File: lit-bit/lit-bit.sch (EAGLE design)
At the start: 71 parts, among them J2 USB_MICRO_B_SMD_FEMALE, J3 ISP, U2 32U4, U3 73831, U4 ADXL345, U5 S-1335, U6 MCP7940N, U7 24FC1025, Y1 8MHz, Y2 32.768kHz, Y3 32.768kHz, Y4 16MHz

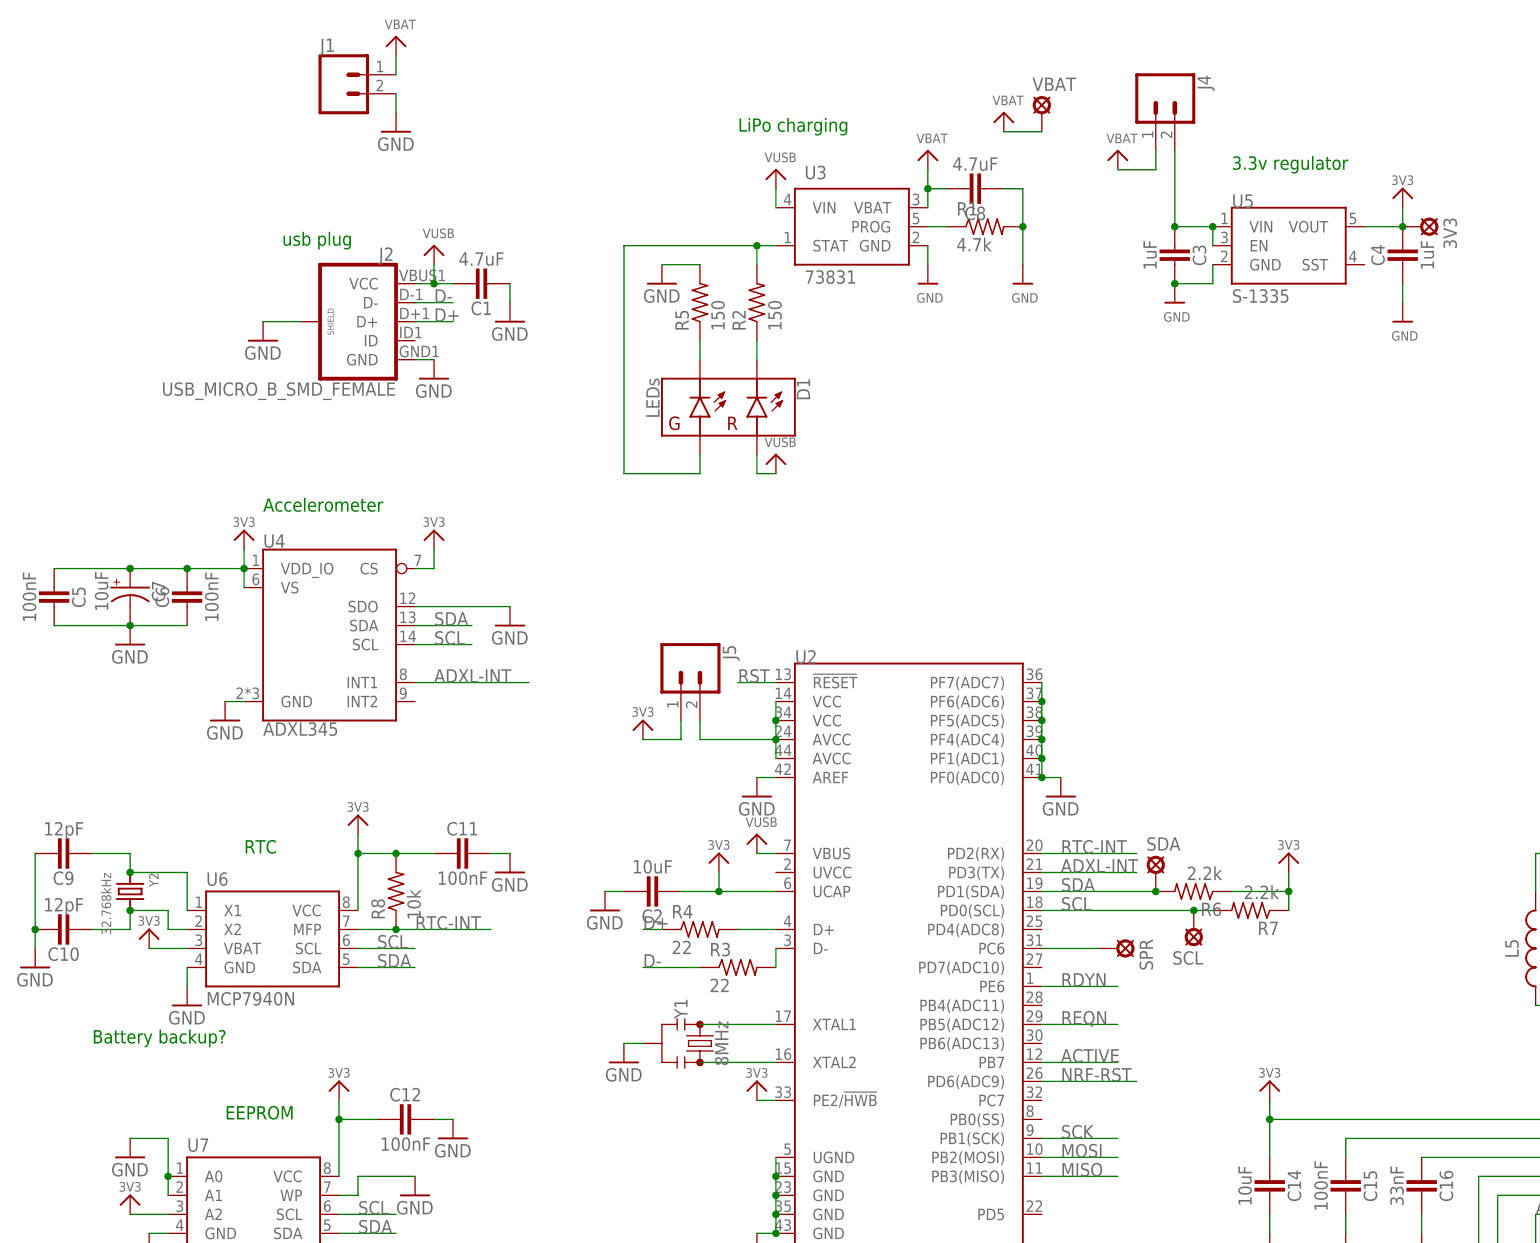
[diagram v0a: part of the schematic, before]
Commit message: almost routed, but not working
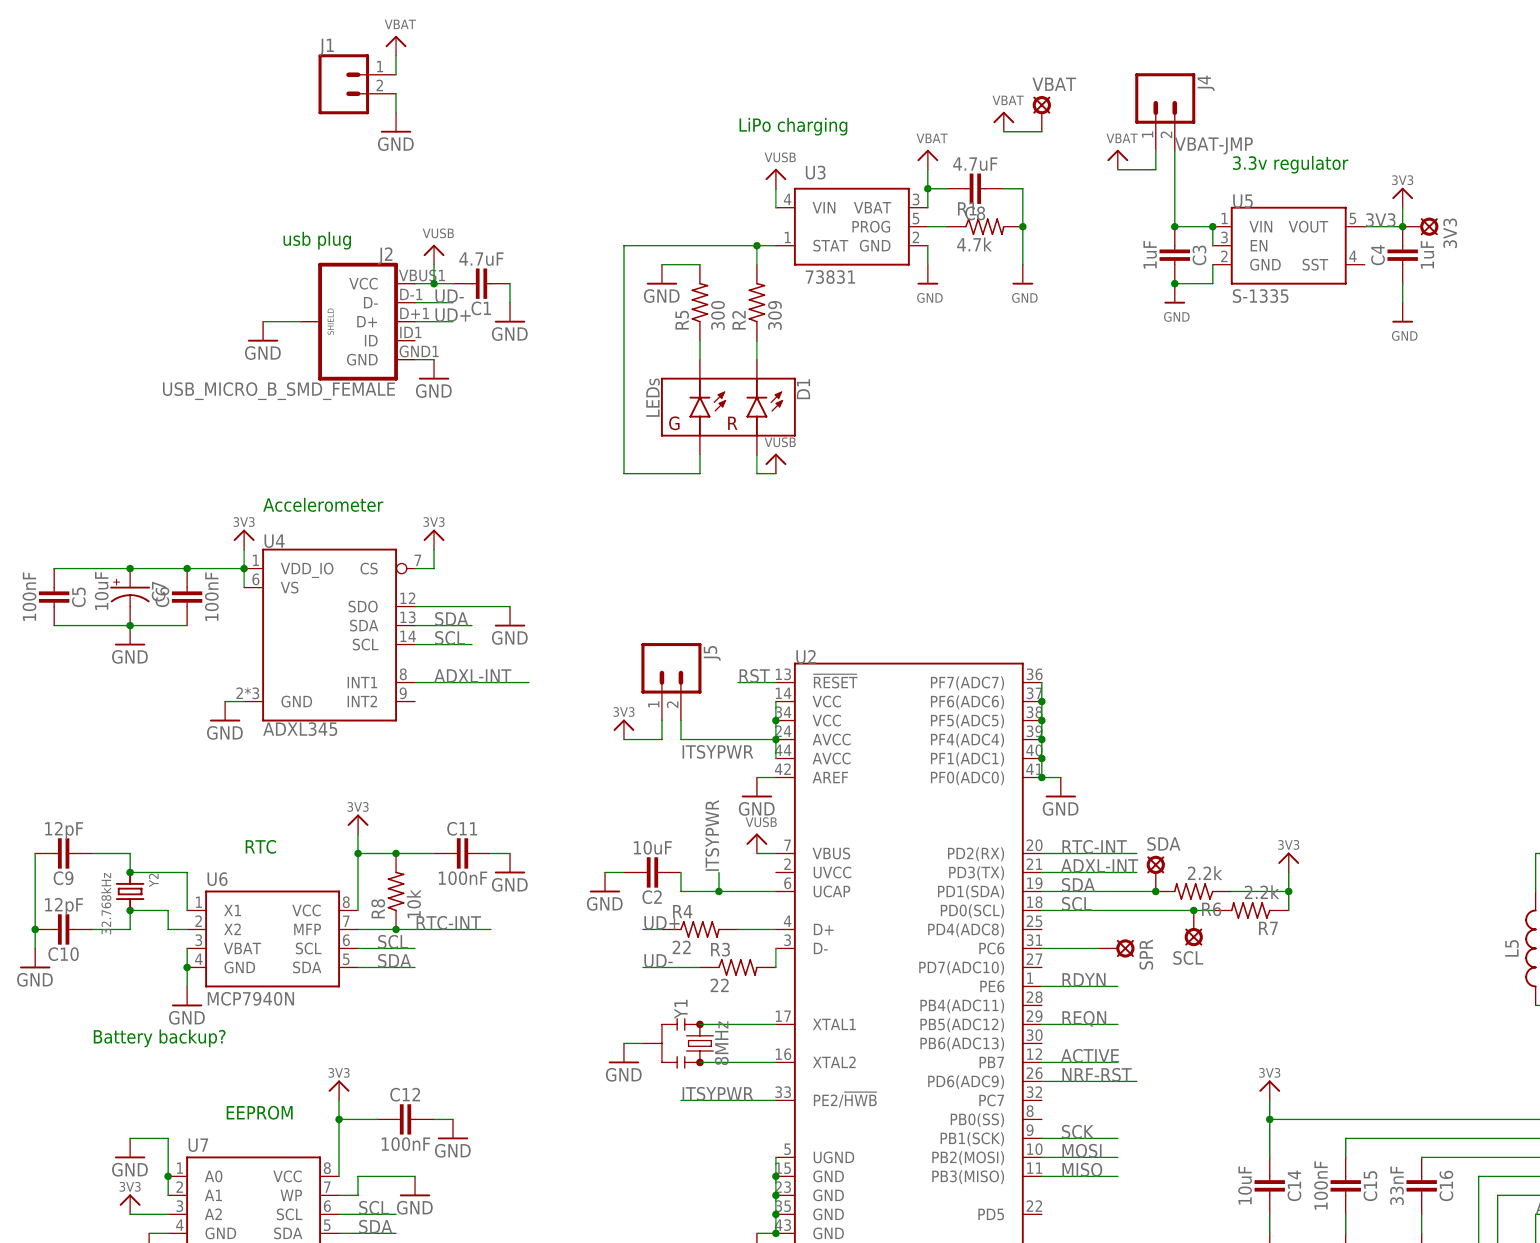
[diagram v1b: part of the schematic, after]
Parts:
- R2: value 150 -> 309
- R5: value 150 -> 300
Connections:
- net D- renamed UD-
- net N$41 renamed VBAT-JMP
- removed net +3V3: 3V3.MP, C11.2, C12.2, C14.2, C19.2, C2.2, C21.2, C4.1, C5.2, C6.1, C7.+, J5.2, JP1.3, R6.1, R7.1, R8.2, U1A.VDD@1, U1A.VDD@2, U2.AVCC@24, U2.AVCC@44, U2.PE2/!HWB, U2.UCAP, U2.VCC@14, U2.VCC@34, U4.CS, U4.VDD_IO, U4.VS, U5.VOUT, U6.VBAT, U6.VCC, U7.A2, U7.VCC
- new net ITSYPWR: C2.2, J5.2, U2.AVCC@24, U2.AVCC@44, U2.PE2/!HWB, U2.UCAP, U2.VCC@14, U2.VCC@34
- new net UD+: J2.D+, R4.1
- net 3V3: now also 3V3.MP, C11.2, C12.2, C14.2, C19.2, C21.2, C4.1, C5.2, C6.1, C7.+, JP1.3, R6.1, R7.1, R8.2, U1A.VDD@1, U1A.VDD@2, U4.CS, U4.VDD_IO, U4.VS, U5.VOUT, U6.VCC, U7.A2, U7.VCC
- net D+: no longer J2.D+, R4.1
- net GND: now also U6.VBAT
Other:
- moved on the sheet: C2, J5

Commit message: reworking
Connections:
- net ACTIVE: no longer R10.1
- net RDYN: now also R10.1
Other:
- moved on the sheet: R10
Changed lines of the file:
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@@
 <instance part="3V3" gate="1" x="165.1" y="177.8" rot="R270"/>
 <instance part="SPR" gate="1" x="124.46" y="81.28" rot="R270"/>
-<instance part="R10" gate="G$1" x="170.18" y="5.08" rot="R90"/>
-<instance part="+3V1" gate="G$1" x="170.18" y="15.24"/>
+<instance part="R10" gate="G$1" x="228.6" y="22.86"/>
+<instance part="+3V1" gate="G$1" x="233.68" y="27.94"/>
 <instance part="U$1" gate="G$1" x="33.02" y="175.26"/>
 <instance part="U$2" gate="G$1" x="78.74" y="185.42"/>
@@
 <wire x1="190.5" y1="45.72" x2="180.34" y2="45.72" width="0.1524" layer="91"/>
 <label x="180.34" y="45.72" size="1.778" layer="95"/>
-<pinref part="R10" gate="G$1" pin="1"/>
-<wire x1="180.34" y1="45.72" x2="180.34" y2="0" width="0.1524" layer="91"/>
-<wire x1="180.34" y1="0" x2="170.18" y2="0" width="0.1524" layer="91"/>
 </segment>
 <segment>
@@
 <wire x1="220.98" y1="30.48" x2="220.98" y2="22.86" width="0.1524" layer="91"/>
 <label x="220.98" y="22.86" size="1.778" layer="95" rot="R90"/>
+<pinref part="R10" gate="G$1" pin="1"/>
+<wire x1="223.52" y1="22.86" x2="220.98" y2="22.86" width="0.1524" layer="91"/>
 </segment>
 <segment>
@@
 <pinref part="+3V1" gate="G$1" pin="3V3"/>
 <pinref part="R10" gate="G$1" pin="2"/>
-<wire x1="170.18" y1="12.7" x2="170.18" y2="10.16" width="0.1524" layer="91"/>
-</segment>
-<segment>
+<wire x1="233.68" y1="25.4" x2="233.68" y2="22.86" width="0.1524" layer="91"/>
+</segment>
+<segment>

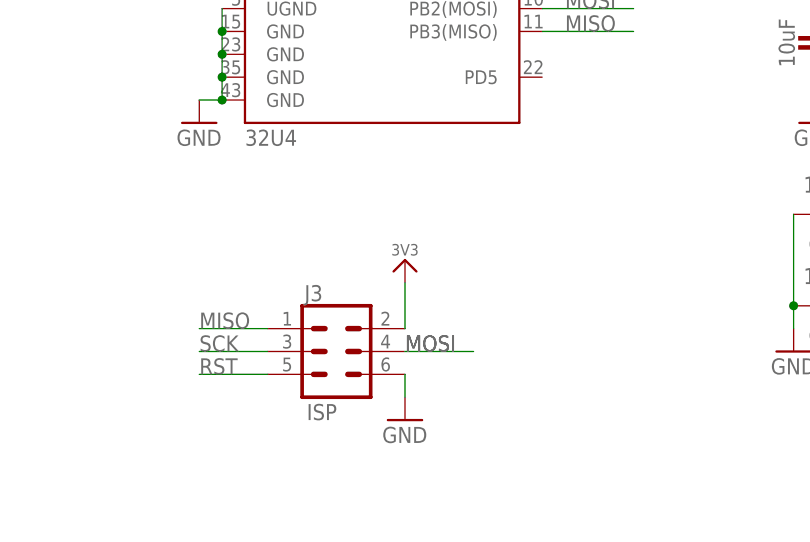
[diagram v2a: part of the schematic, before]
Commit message: routed the bluetooth module successfully
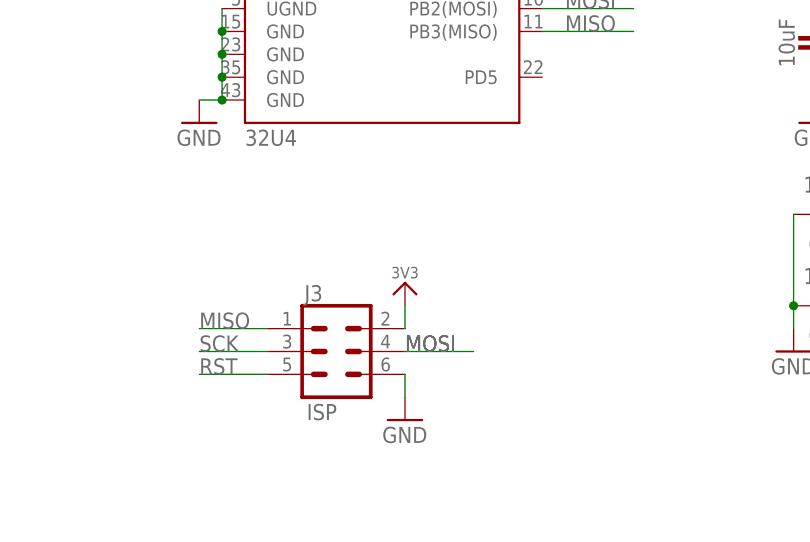
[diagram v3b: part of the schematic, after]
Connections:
- removed net N$26: J3.2
- net 3V3: now also J3.2
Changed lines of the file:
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@@
 <setting verticaltext="up"/>
 </settings>
-<grid distance="0.1" unitdist="inch" unit="inch" style="dots" multiple="1" display="yes" altdistance="0.01" altunitdist="inch" altunit="inch"/>
+<grid distance="0.1" unitdist="inch" unit="inch" style="lines" multiple="1" display="no" altdistance="0.01" altunitdist="inch" altunit="inch"/>
 <layers>
 <layer number="1" name="Top" color="4" fill="1" visible="no" active="no"/>
@@
 <part name="J2" library="SCADA_CUSTOM_LIBRARY" deviceset="USB_MICRO_B_SMD_FEMALE" device=""/>
 <part name="J3" library="SCADA_CUSTOM_LIBRARY" deviceset="CONN_03X2" device="SMT" value="ISP"/>
-<part name="+3V12" library="SCADA_CUSTOM_LIBRARY" deviceset="3V3" device=""/>
 <part name="GND20" library="supply1" library_urn="urn:adsk.eagle:library:371" deviceset="GND" device=""/>
 <part name="U4" library="SCADA_CUSTOM_LIBRARY" deviceset="ADXL345" device=""/>
@@
 <part name="R3" library="SCADA_CUSTOM_LIBRARY" deviceset="RES-0603" device="" value="22"/>
 <part name="R4" library="SCADA_CUSTOM_LIBRARY" deviceset="RES-0603" device="" value="22"/>
+<part name="+3V2" library="SCADA_CUSTOM_LIBRARY" deviceset="3V3" device=""/>
 </parts>
 <sheets>
@@
 <instance part="J2" gate="G$1" x="22.86" y="165.1" rot="MR0"/>
 <instance part="J3" gate="G$1" x="91.44" y="15.24"/>
-<instance part="+3V12" gate="G$1" x="99.06" y="25.4"/>
 <instance part="GND20" gate="1" x="99.06" y="7.62"/>
 <instance part="U4" gate="G$1" x="10.16" y="111.76"/>
@@
 <instance part="R3" gate="G$1" x="73.66" y="78.74"/>
 <instance part="R4" gate="G$1" x="68.58" y="83.82"/>
+<instance part="+3V2" gate="G$1" x="99.06" y="22.86"/>
 </instances>
 <busses>
@@
 </segment>
 </net>
-<net name="N$26" class="0">
-<segment>
-<pinref part="J3" gate="G$1" pin="2"/>
-<wire x1="99.06" y1="17.78" x2="99.06" y2="22.86" width="0.1524" layer="91"/>
-<pinref part="+3V12" gate="G$1" pin="3V3"/>
-</segment>
-</net>
 <net name="N$16" class="0">
 <segment>
@@
 <junction x="15.24" y="17.78"/>
 </segment>
-</net>
+<segment>
+<pinref part="+3V2" gate="G$1" pin="3V3"/>
+<pinref part="J3" gate="G$1" pin="2"/>
+<wire x1="99.06" y1="20.32" x2="99.06" y2="17.78" width="0.1524" layer="91"/>
+</segment>
+</net>

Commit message: fukky routed, but is ugly
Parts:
- J3: device SCADA_CUSTOM_LIBRARY:CONN_03X2SMT -> SCADA_CUSTOM_LIBRARY:CONN_03X22X3_SILK_MALE_PTH
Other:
- note removed: "Battery backup?"
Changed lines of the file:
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@@
 <part name="U6" library="SCADA_CUSTOM_LIBRARY" deviceset="MCP7940N" device=""/>
 <part name="J2" library="SCADA_CUSTOM_LIBRARY" deviceset="USB_MICRO_B_SMD_FEMALE" device=""/>
-<part name="J3" library="SCADA_CUSTOM_LIBRARY" deviceset="CONN_03X2" device="SMT" value="ISP"/>
+<part name="J3" library="SCADA_CUSTOM_LIBRARY" deviceset="CONN_03X2" device="2X3_SILK_MALE_PTH" value="ISP"/>
 <part name="GND20" library="supply1" library_urn="urn:adsk.eagle:library:371" deviceset="GND" device=""/>
 <part name="U4" library="SCADA_CUSTOM_LIBRARY" deviceset="ADXL345" device=""/>
@@
 <text x="73.66" y="190.5" size="1.778" layer="91">LiPo charging</text>
 <text x="139.7" y="185.42" size="1.778" layer="91">3.3v regulator</text>
-<text x="-12.7" y="68.58" size="1.778" layer="91">Battery backup?</text>
 <text x="7.62" y="93.98" size="1.778" layer="91">RTC</text>
 <text x="10.16" y="139.7" size="1.778" layer="91">Accelerometer</text>
@@
 </segment>
 </net>
-<net name="VUSB" class="1">
+<net name="VUSB" class="0">
 <segment>
 <pinref part="D1" gate="G$1" pin="RA"/>
@@
 </sheet>
 </sheets>
+<errors>
+</errors>
 </schematic>
 </drawing>

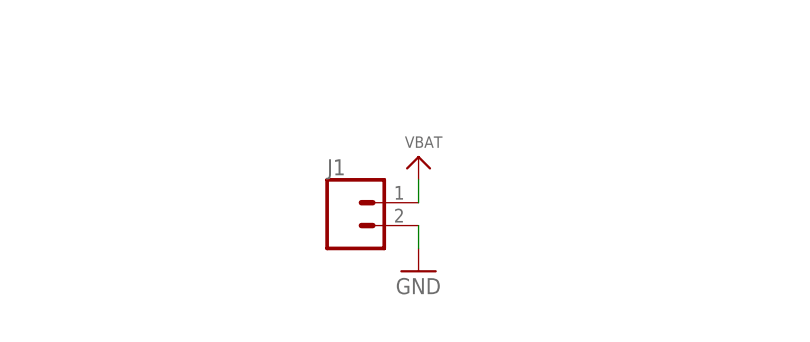
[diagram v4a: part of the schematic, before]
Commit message: added gnd point for testing
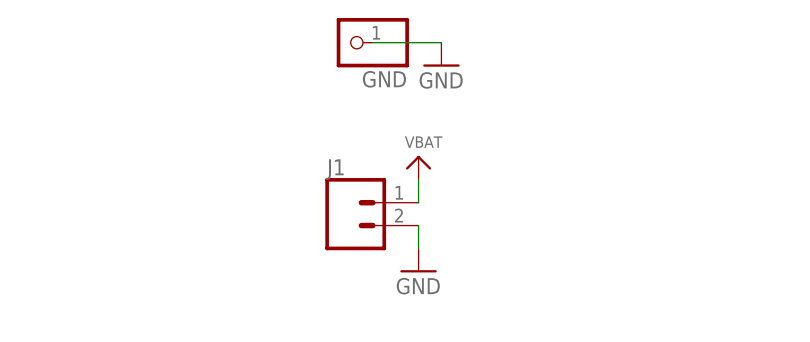
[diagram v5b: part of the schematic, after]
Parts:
- added GND: (no value), microbuilder:HEADER-1X1ROUND
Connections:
- net GND: now also GND.1
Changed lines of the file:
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@@
 <part name="R4" library="SCADA_CUSTOM_LIBRARY" deviceset="RES-0603" device="" value="22"/>
 <part name="+3V2" library="SCADA_CUSTOM_LIBRARY" deviceset="3V3" device=""/>
+<part name="GND" library="microbuilder" deviceset="HEADER-1X1" device="ROUND"/>
+<part name="GND39" library="supply1" library_urn="urn:adsk.eagle:library:371" deviceset="GND" device=""/>
 </parts>
 <sheets>
@@
 <instance part="R4" gate="G$1" x="68.58" y="83.82"/>
 <instance part="+3V2" gate="G$1" x="99.06" y="22.86"/>
+<instance part="GND" gate="G$1" x="20.32" y="215.9" rot="R180"/>
+<instance part="GND39" gate="1" x="30.48" y="213.36"/>
 </instances>
 <busses>
@@
 <wire x1="2.54" y1="25.4" x2="7.62" y2="25.4" width="0.1524" layer="91"/>
 </segment>
+<segment>
+<pinref part="GND" gate="G$1" pin="1"/>
+<wire x1="22.86" y1="215.9" x2="30.48" y2="215.9" width="0.1524" layer="91"/>
+<pinref part="GND39" gate="1" pin="GND"/>
+</segment>
 </net>
